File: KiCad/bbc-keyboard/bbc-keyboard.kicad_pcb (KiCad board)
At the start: 2 copper layers, 337.8 x 137.2 mm, 121 parts, among them IC1 74LS161, IC2 74251, IC3 74145, IC4 74LS30, SW1 escape, SW10 W, SW11 2, SW12 A, SW13 S, SW14 Z, SW15 f2, SW16 4, SW17 E, SW18 D, SW19 X, SW2 Q, SW20 C, SW21 space, SW22 f3, SW23 5, SW24 T, SW25 R, SW26 F, SW27 G, SW28 V, SW29 f5, SW3 F0, SW30 F4, SW31 7, SW32 6, SW33 Y, SW34 H, SW35 B, SW36 f6, SW37 8, SW38 9, SW39 U, SW4 1, SW40 J, SW41 N, SW42 M, SW43 f8, SW44 f7, SW45 I, SW46 O, SW47 K, SW48 L, SW49 <,, SW5 caps lk, SW50 f9, SW51 =-, SW52 0, SW53 P, SW54 @, SW55 ;+, SW56 >., SW57 \|, SW58 ~^, SW59 _£, SW6 shift lk, SW60 {[, SW61 *:, SW62 }], SW63 ?/, SW64 right, SW65 left, SW66 down, SW67 up, SW68 return, SW69 delete, SW7 tab, SW70 copy, SW71 shift, SW72 shift, SW73 ctrl, SW74 SW_DIP_x08, SW75 break, SW8 f1, SW9 3

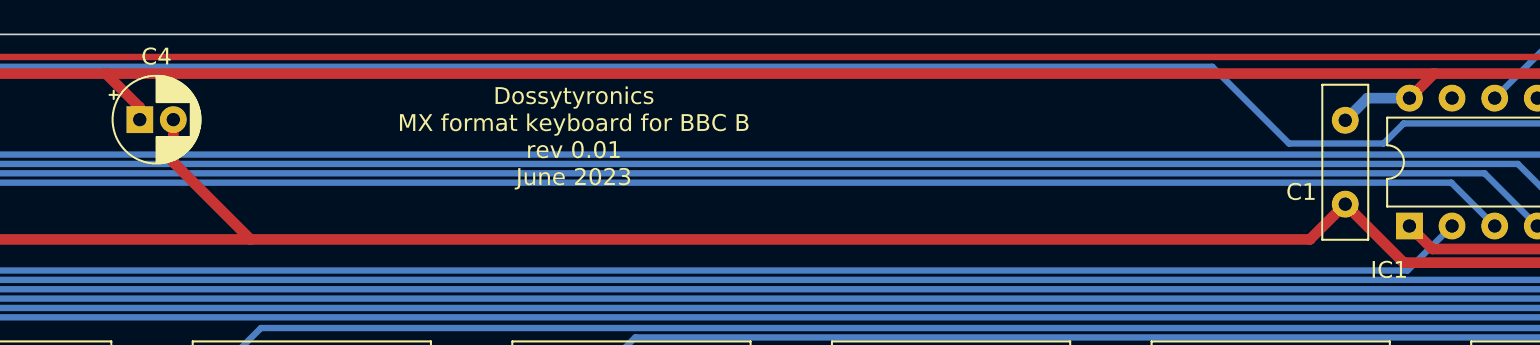
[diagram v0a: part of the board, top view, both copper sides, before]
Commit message: rotate C4 - allow bend horizontally
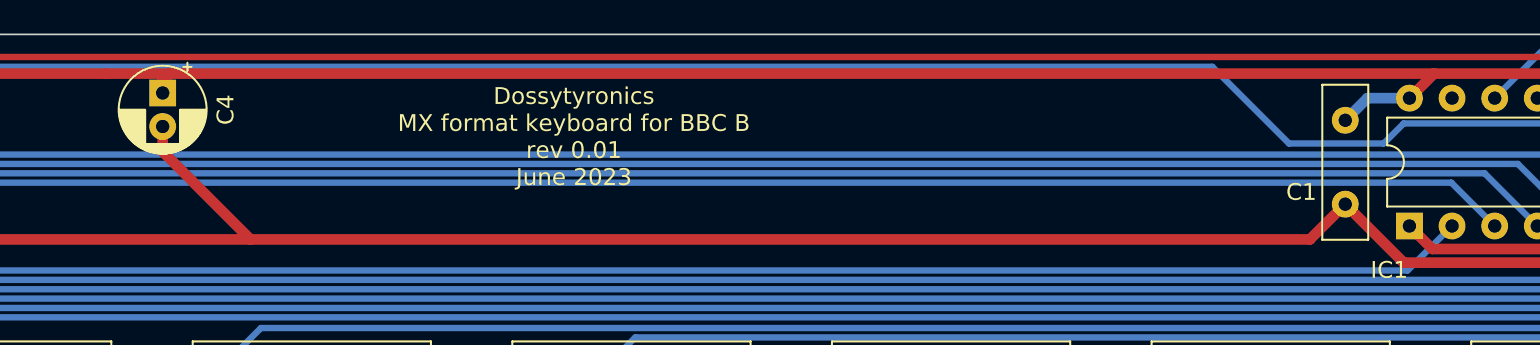
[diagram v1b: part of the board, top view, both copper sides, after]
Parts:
- moved C4 2.10 mm to (224.5, 98.7), turned to -90 degrees
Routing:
- net VCC: track 552.7 -> 550.5 mm
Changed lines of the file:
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@@
   )
   (footprint "Capacitor_THT:CP_Radial_D5.0mm_P2.00mm" (layer "F.Cu")
-    (at 223.1075 100.33)
+    (at 224.4725 98.739888 -90)
     (descr "CP, Radial series, Radial, pin pitch=2.00mm, , diameter=5mm, Electrolytic Capacitor")
     (tags "CP Radial series Radial pin pitch 2.00mm  diameter 5mm Electrolytic Capacitor")
@@
     (property "Sheetname" "")
     (attr through_hole)
-    (fp_text reference "C4" (at 1 -3.75) (layer "F.SilkS")
-      (effects (font (size 1 1) (thickness 0.15)))
-    )
-    (fp_text value "22u" (at 1 3.75) (layer "F.Fab")
-      (effects (font (size 1 1) (thickness 0.15)))
-    )
-    (fp_text user "${REFERENCE}" (at 1 0) (layer "F.Fab")
+    (fp_text reference "C4" (at 1 -3.75 90) (layer "F.SilkS")
+      (effects (font (size 1 1) (thickness 0.15)))
+    )
+    (fp_text value "22u" (at 1 3.75 90) (layer "F.Fab")
+      (effects (font (size 1 1) (thickness 0.15)))
+    )
+    (fp_text user "${REFERENCE}" (at 1 0 90) (layer "F.Fab")
       (effects (font (size 1 1) (thickness 0.15)))
     )
@@
     (fp_line (start -0.883605 -1.3375) (end -0.883605 -0.8375) (layer "F.Fab") (width 0.1))
     (fp_circle (center 1 0) (end 3.5 0) (layer "F.Fab") (width 0.1) (fill none))
-    (pad "1" thru_hole rect locked (at 0 0) (size 1.6 1.6) (drill 0.8) (layers *.Cu *.Mask)
+    (pad "1" thru_hole rect locked (at 0 0 270) (size 1.6 1.6) (drill 0.8) (layers *.Cu *.Mask)
       (net 1 "VCC") (pintype "passive"))
-    (pad "2" thru_hole circle locked (at 2 0) (size 1.6 1.6) (drill 0.8) (layers *.Cu *.Mask)
+    (pad "2" thru_hole circle locked (at 2 0 270) (size 1.6 1.6) (drill 0.8) (layers *.Cu *.Mask)
       (net 22 "GND") (pintype "passive"))
     (model "${KICAD6_3DMODEL_DIR}/Capacitor_THT.3dshapes/CP_Radial_D5.0mm_P2.00mm.wrl"
@@
   )
   (segment (start 306.772691 108.041899) (end 306.924995 107.889596) (width 0.635) (layer "F.Cu") (net 1))
+  (segment (start 224.4725 98.0186) (end 224.9043 97.5868) (width 0.635) (layer "F.Cu") (net 1))
   (segment (start 117.439999 101.317501) (end 117.439999 102.028701) (width 0.635) (layer "F.Cu") (net 1))
   (segment (start 70.1675 226.06) (end 114.6175 226.06) (width 0.635) (layer "F.Cu") (net 1))
@@
   (segment (start 158.7119 101.3968) (end 133.4243 101.3968) (width 0.635) (layer "F.Cu") (net 1))
   (segment (start 308.415405 107.965796) (end 312.726704 107.965796) (width 0.635) (layer "F.Cu") (net 1))
+  (segment (start 300.2457 97.5868) (end 224.9043 97.5868) (width 0.635) (layer "F.Cu") (net 1))
   (segment (start 353.3775 100.37) (end 353.3775 97.79) (width 0.635) (layer "F.Cu") (net 1))
   (segment (start 133.7175 99.05) (end 131.5231 101.2444) (width 0.635) (layer "F.Cu") (net 1))
@@
   (segment (start 71.6915 129.286) (end 47.6885 153.289) (width 0.635) (layer "F.Cu") (net 1))
   (segment (start 47.6885 153.289) (end 47.6885 203.581) (width 0.635) (layer "F.Cu") (net 1))
+  (segment (start 224.9043 97.5868) (end 221.0943 97.5868) (width 0.635) (layer "F.Cu") (net 1))
   (segment (start 221.0943 97.5868) (end 199.2007 97.5868) (width 0.635) (layer "F.Cu") (net 1))
   (segment (start 197.1625 99.625) (end 191.8601 104.9274) (width 0.635) (layer "F.Cu") (net 1))
@@
   (segment (start 353.3775 97.79) (end 353.8093 97.3582) (width 0.635) (layer "F.Cu") (net 1))
   (segment (start 308.339206 107.889596) (end 308.415405 107.965796) (width 0.635) (layer "F.Cu") (net 1))
-  (segment (start 223.1075 99.6) (end 221.0943 97.5868) (width 0.635) (layer "F.Cu") (net 1))
   (segment (start 298.7825 106.67) (end 300.154399 108.041899) (width 0.635) (layer "F.Cu") (net 1))
   (segment (start 315.7143 97.3582) (end 314.0225 99.05) (width 0.635) (layer "F.Cu") (net 1))
-  (segment (start 223.1075 100.33) (end 223.1075 99.6) (width 0.635) (layer "F.Cu") (net 1))
-  (segment (start 300.2457 97.5868) (end 221.0943 97.5868) (width 0.635) (layer "F.Cu") (net 1))
   (segment (start 359.4481 101.3206) (end 357.1825 99.055) (width 0.635) (layer "F.Cu") (net 1))
   (segment (start 117.439999 102.028701) (end 105.2128 114.2559) (width 0.635) (layer "F.Cu") (net 1))
@@
   (segment (start 314.0225 106.67) (end 314.0225 99.05) (width 0.635) (layer "F.Cu") (net 1))
   (segment (start 191.8601 104.9274) (end 190.4873 104.9274) (width 0.635) (layer "F.Cu") (net 1))
+  (segment (start 224.4725 98.739888) (end 224.4725 98.0186) (width 0.635) (layer "F.Cu") (net 1))
   (segment (start 312.5593 97.5868) (end 300.2457 97.5868) (width 0.635) (layer "F.Cu") (net 1))
   (segment (start 99.6569 119.950858) (end 99.6569 125.8062) (width 0.635) (layer "F.Cu") (net 1))
@@
   (segment (start 112.0013 119.3038) (end 102.2477 119.3038) (width 0.635) (layer "F.Cu") (net 22))
   (segment (start 234.5817 202.6158) (end 249.6185 202.6158) (width 0.635) (layer "F.Cu") (net 22))
+  (segment (start 224.4725 100.739888) (end 224.4725 102.235) (width 0.635) (layer "F.Cu") (net 22))
   (segment (start 185.7375 213.36) (end 185.7375 217.6272) (width 0.635) (layer "F.Cu") (net 22))
   (segment (start 163.9443 223.7232) (end 160.3883 227.2792) (width 0.635) (layer "F.Cu") (net 22))
@@
   (segment (start 71.9455 150.622) (end 85.9663 150.622) (width 0.635) (layer "F.Cu") (net 22))
   (segment (start 348.1605 106.67) (end 345.7725 106.67) (width 0.635) (layer "F.Cu") (net 22))
-  (segment (start 225.1075 100.33) (end 225.1075 102.87) (width 0.635) (layer "F.Cu") (net 22))
   (segment (start 350.8375 229.87) (end 363.5375 217.17) (width 0.635) (layer "F.Cu") (net 22))
   (segment (start 132.3975 105.37) (end 152.7025 105.37) (width 0.635) (layer "F.Cu") (net 22))
@@
   (segment (start 367.3475 213.36) (end 367.3475 191.77) (width 0.635) (layer "F.Cu") (net 22))
   (segment (start 185.7375 217.6272) (end 191.8335 223.7232) (width 0.635) (layer "F.Cu") (net 22))
-  (segment (start 225.1075 102.87) (end 229.707499 107.469999) (width 0.635) (layer "F.Cu") (net 22))
   (segment (start 213.4743 223.7232) (end 234.5817 202.6158) (width 0.635) (layer "F.Cu") (net 22))
   (segment (start 51.1175 227.33) (end 53.6575 229.87) (width 0.635) (layer "F.Cu") (net 22))
@@
   (segment (start 51.1175 217.17) (end 56.1975 217.17) (width 0.635) (layer "F.Cu") (net 22))
   (segment (start 53.6575 229.87) (end 120.9675 229.87) (width 0.635) (layer "F.Cu") (net 22))
+  (segment (start 224.4725 102.235) (end 229.707499 107.469999) (width 0.635) (layer "F.Cu") (net 22))
   (segment (start 341.9475 118.11) (end 350.3549 109.7026) (width 0.635) (layer "F.Cu") (net 22))
   (segment (start 308.002739 108.701897) (end 308.155042 108.8542) (width 0.635) (layer "F.Cu") (net 22))

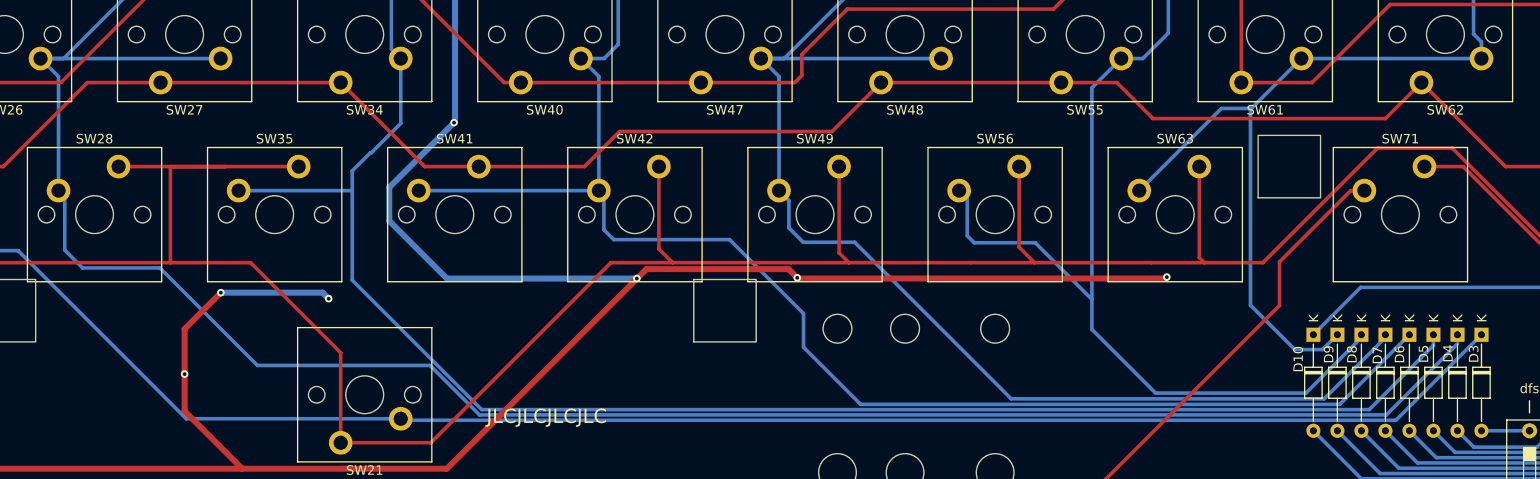
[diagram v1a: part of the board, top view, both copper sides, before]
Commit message: increase clearance around diode array
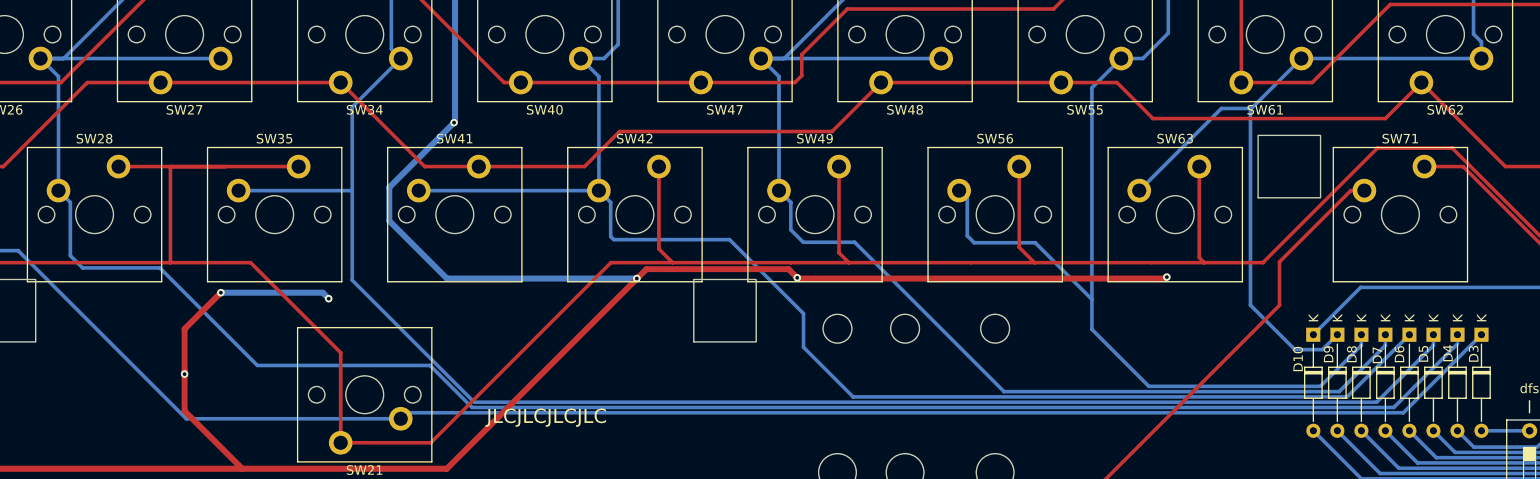
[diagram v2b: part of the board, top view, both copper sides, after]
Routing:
- net /Key Matrix/KC_COL4: track 394.5 -> 393.8 mm
- net /Key Matrix/KC_COL3: track 452.8 -> 452.2 mm
- net /Key Matrix/KC_COL5: track 335.4 -> 334.8 mm
